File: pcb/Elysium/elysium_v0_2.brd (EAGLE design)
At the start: 64.8 x 105.1 mm, 14 parts, among them U1 TLC5940-NT, U2 TLC5940-NT, U3 TLC5940-NT, U4 TLC5940-NT

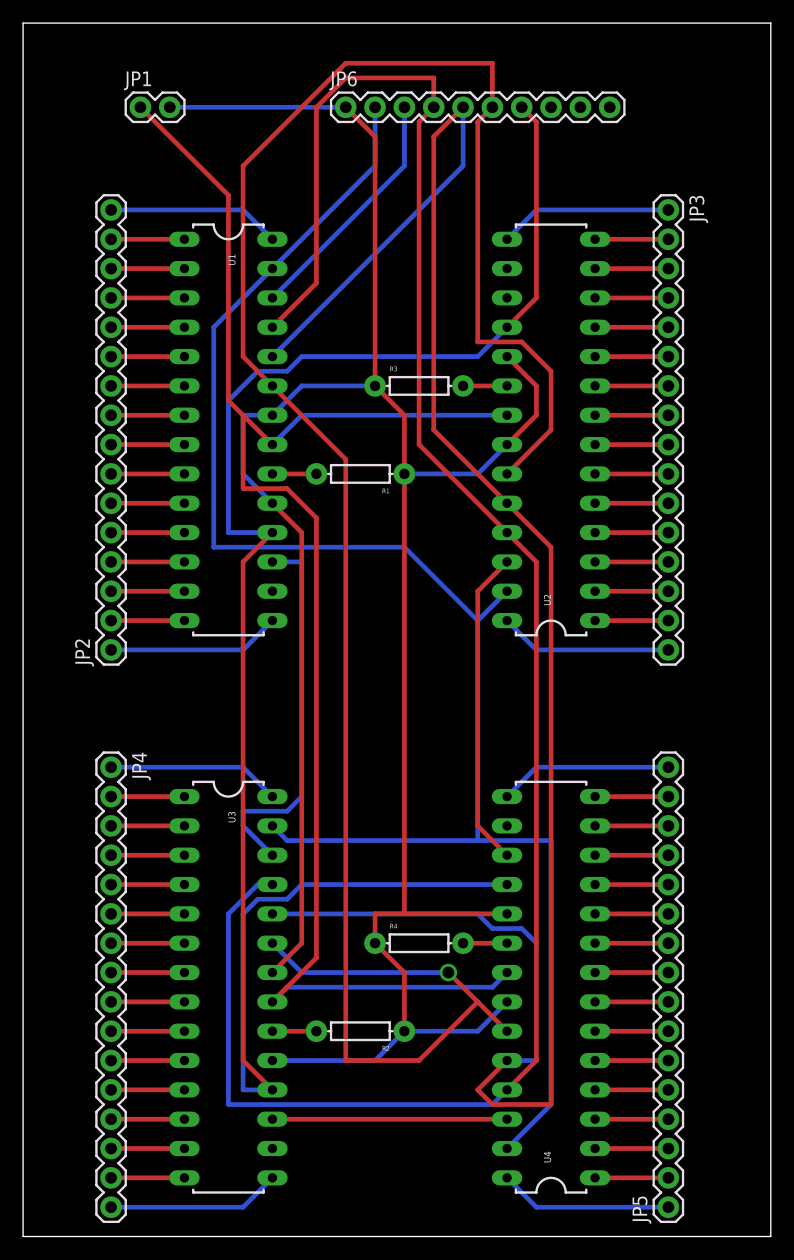
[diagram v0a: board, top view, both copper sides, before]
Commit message: Added rev_0_4 board
Rev 0_4 has status LEDs with ground planes.
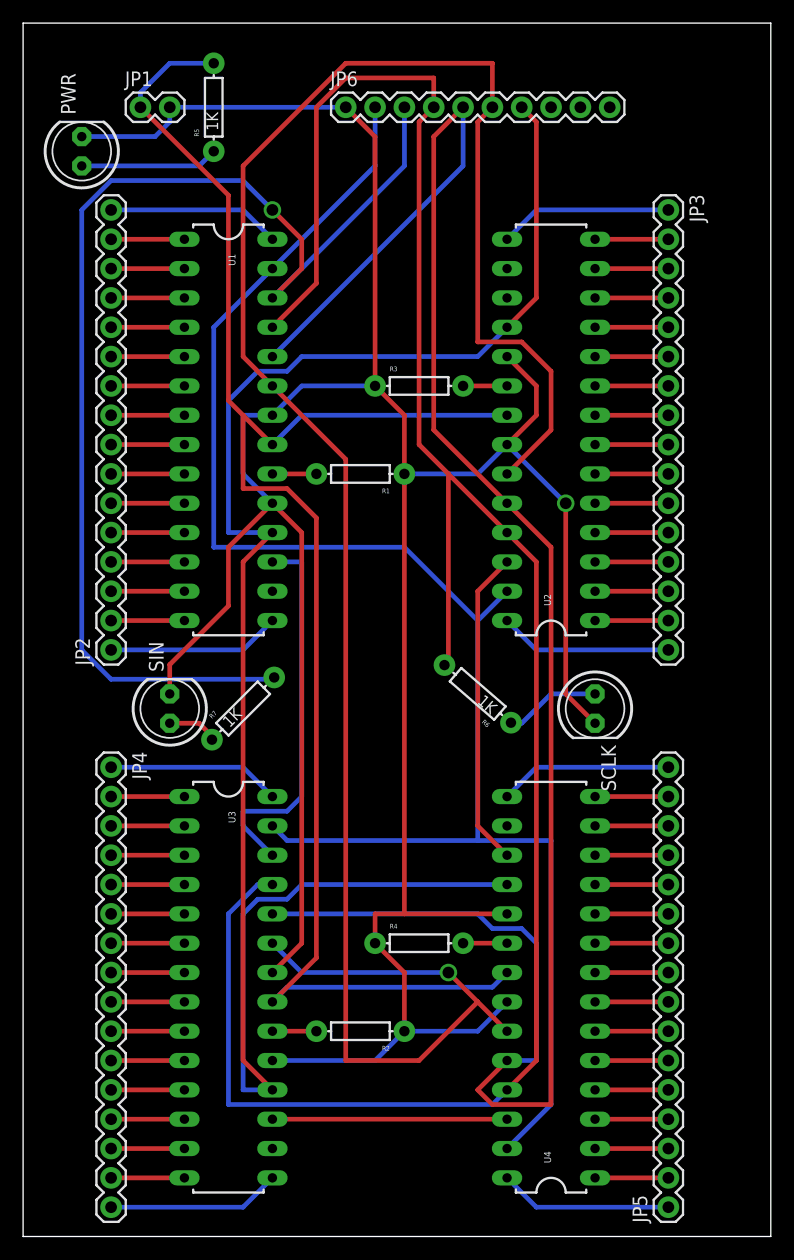
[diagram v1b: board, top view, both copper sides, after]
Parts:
- added PWR, SCLK, SIN: (no value), adafruit:LED5MM
- added R5, R6, R7: 1K, SparkFun-Resistors:AXIAL-0.3EZ
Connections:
- new net N$69: PWR.A, R5.P$1
- new net N$74: R6.P$1, SCLK.A
- new net N$76: R7.P$1, SIN.A
- net GND: now also PWR.K, SCLK.K, SIN.K
- net SCLK: now also R6.P$2
- net SIN: now also R7.P$2
- net VCC: now also R5.P$2
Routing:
- net SIN: track 21.2 -> 105.5 mm, vias 0 -> 1
- net GND: track 215.8 -> 272.7 mm, vias 0 -> 1
- net SCLK: track 171.3 -> 188.1 mm
- net N$69: track 0.00 -> 12.0 mm
- net VCC: track 133.9 -> 142.6 mm
- net N$74: track 0.00 -> 8.33 mm
- net N$76: track 0.00 -> 4.55 mm
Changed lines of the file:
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@@
 <layer number="54" name="bGND_GNDA" color="1" fill="9" visible="no" active="no"/>
 <layer number="56" name="wert" color="7" fill="1" visible="no" active="no"/>
+<layer number="57" name="tCAD" color="7" fill="1" visible="no" active="no"/>
 <layer number="91" name="Nets" color="2" fill="1" visible="no" active="no"/>
 <layer number="92" name="Busses" color="1" fill="1" visible="no" active="no"/>
@@
 <layer number="108" name="tplace-old" color="10" fill="1" visible="yes" active="yes"/>
 <layer number="109" name="ref-old" color="11" fill="1" visible="yes" active="yes"/>
+<layer number="110" name="fp0" color="7" fill="1" visible="no" active="yes"/>
+<layer number="111" name="LPC17xx" color="7" fill="1" visible="yes" active="yes"/>
+<layer number="112" name="tSilk" color="7" fill="1" visible="yes" active="yes"/>
 <layer number="116" name="Patch_BOT" color="9" fill="4" visible="yes" active="yes"/>
 <layer number="121" name="_tsilk" color="7" fill="1" visible="yes" active="yes"/>
 <layer number="122" name="_bsilk" color="7" fill="1" visible="yes" active="yes"/>
+<layer number="123" name="tTestmark" color="7" fill="1" visible="no" active="yes"/>
+<layer number="124" name="bTestmark" color="7" fill="1" visible="no" active="yes"/>
 <layer number="125" name="_tNames" color="7" fill="1" visible="yes" active="yes"/>
+<layer number="126" name="_bNames" color="7" fill="1" visible="yes" active="yes"/>
+<layer number="127" name="_tValues" color="7" fill="1" visible="yes" active="yes"/>
+<layer number="128" name="_bValues" color="7" fill="1" visible="yes" active="yes"/>
+<layer number="131" name="tAdjust" color="7" fill="1" visible="no" active="yes"/>
+<layer number="132" name="bAdjust" color="7" fill="1" visible="no" active="yes"/>
 <layer number="144" name="Drill_legend" color="7" fill="1" visible="yes" active="yes"/>
+<layer number="150" name="Notes" color="7" fill="1" visible="no" active="yes"/>
 <layer number="151" name="HeatSink" color="7" fill="1" visible="yes" active="yes"/>
+<layer number="152" name="_bDocu" color="7" fill="1" visible="yes" active="yes"/>
+<layer number="153" name="FabDoc1" color="6" fill="1" visible="no" active="no"/>
+<layer number="154" name="FabDoc2" color="2" fill="1" visible="no" active="no"/>
+<layer number="155" name="FabDoc3" color="7" fill="15" visible="no" active="no"/>
 <layer number="199" name="Contour" color="7" fill="1" visible="yes" active="yes"/>
 <layer number="200" name="200bmp" color="1" fill="10" visible="yes" active="yes"/>
@@
 <layer number="223" name="223bmp" color="24" fill="1" visible="no" active="no"/>
 <layer number="224" name="224bmp" color="25" fill="1" visible="no" active="no"/>
+<layer number="248" name="Housing" color="7" fill="1" visible="yes" active="yes"/>
+<layer number="249" name="Edge" color="7" fill="1" visible="yes" active="yes"/>
 <layer number="250" name="Descript" color="3" fill="1" visible="no" active="no"/>
 <layer number="251" name="SMDround" color="12" fill="11" visible="no" active="no"/>
@@
 <param name="mdSmdStop" value="0mil"/>
 <param name="msWidth" value="16mil"/>
-<param name="msDrill" value="20mil"/>
+<param name="msDrill" value="40mil"/>
 <param name="msMicroVia" value="9.99mm"/>
 <param name="msBlindViaRatio" value="0.5"/>
@@
 <param name="RoutingGrid" value="50mil"/>
 <param name="tpViaShape" value="round"/>
-<param name="PrefDir.1" value="|"/>
+<param name="PrefDir.1" value="*"/>
 <param name="PrefDir.2" value="0"/>
 <param name="PrefDir.3" value="0"/>
@@
 <param name="PrefDir.14" value="0"/>
 <param name="PrefDir.15" value="0"/>
-<param name="PrefDir.16" value="-"/>
+<param name="PrefDir.16" value="*"/>
 <param name="cfVia" value="8"/>
 <param name="cfNonPref" value="5"/>
@@
 <element name="R3" library="SparkFun-Resistors" package="AXIAL-0.3EZ" value="" x="34.29" y="68.58"/>
 <element name="R4" library="SparkFun-Resistors" package="AXIAL-0.3EZ" value="" x="34.29" y="20.32"/>
+<element name="PWR" library="adafruit" package="LED5MM" value="" x="5.08" y="88.9" rot="R90"/>
+<element name="R5" library="SparkFun-Resistors" package="AXIAL-0.3EZ" value="1K" x="16.51" y="92.71" rot="R90"/>
+<element name="SCLK" library="adafruit" package="LED5MM" value="" x="49.53" y="40.64" rot="R270"/>
+<element name="R6" library="SparkFun-Resistors" package="AXIAL-0.3EZ" value="1K" x="39.37" y="41.91" rot="R139.1"/>
+<element name="SIN" library="adafruit" package="LED5MM" value="" x="12.7" y="40.64" rot="R90"/>
+<element name="R7" library="SparkFun-Resistors" package="AXIAL-0.3EZ" value="1K" x="19.05" y="40.64" rot="R45"/>
 </elements>
 <signals>
@@
 <wire x1="19.05" y1="66.04" x2="19.05" y2="60.96" width="0.4064" layer="16"/>
 <wire x1="21.59" y1="66.04" x2="19.05" y2="66.04" width="0.4064" layer="16"/>
+<contactref element="PWR" pad="K"/>
+<contactref element="SCLK" pad="K"/>
+<contactref element="SIN" pad="K"/>
+<wire x1="5.08" y1="90.17" x2="11.43" y2="90.17" width="0.4064" layer="16"/>
+<wire x1="11.43" y1="90.17" x2="12.7" y2="91.44" width="0.4064" layer="16"/>
+<wire x1="12.7" y1="91.44" x2="12.7" y2="92.71" width="0.4064" layer="16"/>
+<wire x1="12.7" y1="44.45" x2="12.7" y2="41.91" width="0.4064" layer="1"/>
+<wire x1="17.78" y1="49.53" x2="12.7" y2="44.45" width="0.4064" layer="1"/>
+<wire x1="17.78" y1="54.61" x2="17.78" y2="49.53" width="0.4064" layer="1"/>
+<wire x1="21.59" y1="58.42" x2="17.78" y2="54.61" width="0.4064" layer="1"/>
+<wire x1="46.99" y1="41.91" x2="49.53" y2="39.37" width="0.4064" layer="1"/>
+<wire x1="46.99" y1="58.42" x2="46.99" y2="41.91" width="0.4064" layer="1"/>
+<wire x1="41.91" y1="63.5" x2="46.99" y2="58.42" width="0.4064" layer="16"/>
+<via x="46.99" y="58.42" extent="1-16" drill="1.016"/>
 </signal>
 <signal name="VCC">
@@
 <wire x1="19.05" y1="59.69" x2="22.86" y2="59.69" width="0.4064" layer="1"/>
 <wire x1="19.05" y1="66.04" x2="19.05" y2="59.69" width="0.4064" layer="1"/>
+<contactref element="R5" pad="P$2"/>
+<wire x1="10.16" y1="92.71" x2="10.16" y2="93.98" width="0.4064" layer="16"/>
+<wire x1="10.16" y1="93.98" x2="12.7" y2="96.52" width="0.4064" layer="16"/>
+<wire x1="12.7" y1="96.52" x2="16.51" y2="96.52" width="0.4064" layer="16"/>
 </signal>
 <signal name="N$1">
@@
 <wire x1="33.02" y1="87.63" x2="21.59" y2="76.2" width="0.4064" layer="16"/>
 <wire x1="33.02" y1="92.71" x2="33.02" y2="87.63" width="0.4064" layer="16"/>
+<contactref element="R7" pad="P$2"/>
+<wire x1="7.62" y1="43.18" x2="21.59" y2="43.18" width="0.4064" layer="16"/>
+<wire x1="5.08" y1="45.72" x2="7.62" y2="43.18" width="0.4064" layer="16"/>
+<wire x1="5.08" y1="83.82" x2="5.08" y2="45.72" width="0.4064" layer="16"/>
+<wire x1="7.62" y1="86.36" x2="5.08" y2="83.82" width="0.4064" layer="16"/>
+<wire x1="19.05" y1="86.36" x2="7.62" y2="86.36" width="0.4064" layer="16"/>
+<wire x1="21.59" y1="83.82" x2="19.05" y2="86.36" width="0.4064" layer="16"/>
+<wire x1="24.13" y1="81.28" x2="21.59" y2="83.82" width="0.4064" layer="1"/>
+<wire x1="24.13" y1="78.74" x2="24.13" y2="81.28" width="0.4064" layer="1"/>
+<wire x1="21.59" y1="76.2" x2="24.13" y2="78.74" width="0.4064" layer="1"/>
+<wire x1="21.59" y1="43.18" x2="21.744075" y2="43.334075" width="0.4064" layer="16"/>
+<via x="21.59" y="83.82" extent="1-16" drill="1.016"/>
 </signal>
 <signal name="SCLK">
@@
 <wire x1="34.29" y1="91.44" x2="35.56" y2="92.71" width="0.4064" layer="1"/>
 <wire x1="34.29" y1="63.5" x2="34.29" y2="91.44" width="0.4064" layer="1"/>
-<wire x1="41.91" y1="55.88" x2="34.29" y2="63.5" width="0.4064" layer="1"/>
+<wire x1="41.91" y1="55.88" x2="36.83" y2="60.96" width="0.4064" layer="1"/>
+<contactref element="R6" pad="P$2"/>
+<wire x1="36.83" y1="60.96" x2="34.29" y2="63.5" width="0.4064" layer="1"/>
+<wire x1="36.83" y1="60.96" x2="36.83" y2="44.45" width="0.4064" layer="1"/>
+<wire x1="36.83" y1="44.45" x2="36.490196875" y2="44.4045625" width="0.4064" layer="1"/>
 </signal>
 <signal name="GSCLK">
@@
 <wire x1="38.1" y1="20.32" x2="41.91" y2="20.32" width="0.4064" layer="1"/>
 </signal>
+<signal name="N$69">
+<contactref element="R5" pad="P$1"/>
+<contactref element="PWR" pad="A"/>
+<wire x1="5.08" y1="87.63" x2="15.24" y2="87.63" width="0.4064" layer="16"/>
+<wire x1="15.24" y1="87.63" x2="16.51" y2="88.9" width="0.4064" layer="16"/>
+</signal>
+<signal name="N$74">
+<contactref element="R6" pad="P$1"/>
+<contactref element="SCLK" pad="A"/>
+<wire x1="45.72" y1="41.91" x2="49.53" y2="41.91" width="0.4064" layer="16"/>
+<wire x1="43.18" y1="39.37" x2="45.72" y2="41.91" width="0.4064" layer="16"/>
+<wire x1="43.18" y1="39.37" x2="42.2498" y2="39.415434375" width="0.4064" layer="16"/>
+</signal>
+<signal name="N$76">
+<contactref element="SIN" pad="A"/>
+<contactref element="R7" pad="P$1"/>
+<wire x1="15.24" y1="39.37" x2="12.7" y2="39.37" width="0.4064" layer="1"/>
+<wire x1="16.51" y1="38.1" x2="15.24" y2="39.37" width="0.4064" layer="1"/>
+<wire x1="16.51" y1="38.1" x2="16.355921875" y2="37.945921875" width="0.4064" layer="1"/>
+</signal>
 </signals>
